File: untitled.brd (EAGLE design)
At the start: 160 x 100 mm, 33 parts, among them J2 1x3 RA Female .1", U1 SI4463-C2A-GM, U2 ATSAMD21G-M

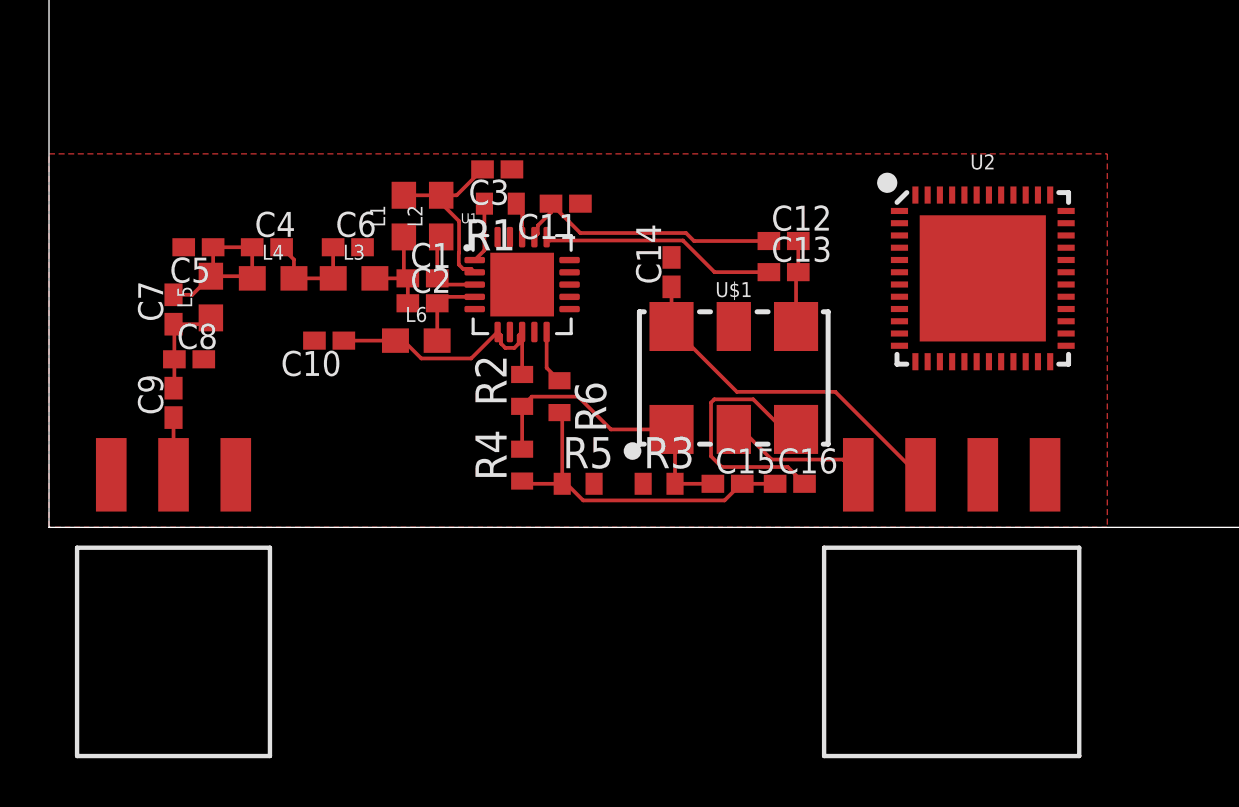
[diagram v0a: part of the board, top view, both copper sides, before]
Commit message: initial atsamd21g schematic capture
added samd21g connections.
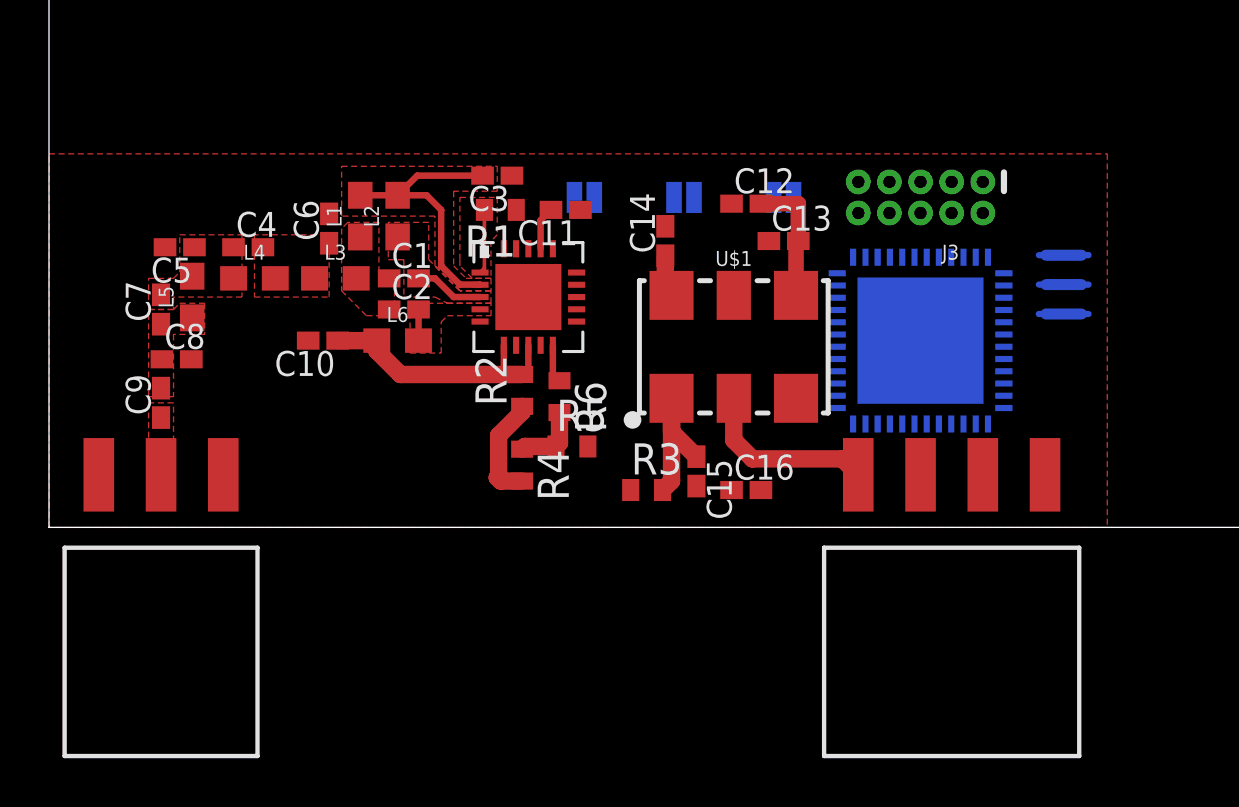
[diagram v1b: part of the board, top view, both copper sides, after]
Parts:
- removed U1: SI4463-C2A-GM, SI4463-C2A-GM:QFN50P400X400X90-20N
- added J3: CORTEX_DEBUG_PTH, SparkFun-Connectors:2X5-PTH-1.27MM
- added REGION1, REGION2, REGION3: JUMPER-SMT_2_NO_SILK, SparkFun-Jumpers:SMT-JUMPER_2_NO_SILK
- added U$2: SI4464, Ava:QFN20+GNDPAD
- added Y1: (no value), SparkFun-Clocks:RESONATOR-SMD-3.2X1.3
- moved U2 3.59 mm to (35.6, 7.62), flipped to the bottom
- moved C12 2.16 mm to (28.4, 13.2)
- moved C16 1.80 mm to (28.4, 1.52)
- moved L1 1.78 mm to (12.7, 12.7)
- moved L2 1.78 mm to (14.2, 12.7)
- moved R5 1.55 mm to (21.3, 3.30)
- moved C15 1.37 mm to (26.4, 2.29), turned to 270 degrees
- moved C14 1.30 mm to (25.1, 11.7)
- moved C13 1.27 mm to (30.0, 11.7)
- moved U$1 1.27 mm to (27.9, 7.37)
- moved C6 1.08 mm to (11.4, 12.2), turned to 90 degrees
- moved C2 0.80 mm to (14.5, 8.89)
- moved C1 0.76 mm to (14.5, 10.2)
- moved C4 0.76 mm to (8.13, 11.4)
- moved C5 0.76 mm to (5.33, 11.4)
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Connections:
- new net !RESET: J3.10, U2.40
- new net A0: U2.3
- new net A1: U2.7
- new net A2: U2.8
- new net A3: U2.9
- new net A4: U2.10
- new net A5: U2.47
- new net AREF: U2.4
- new net D0: U2.16
- new net D1: U2.15
- new net D10: U2.27
- new net D11: U2.25
- new net D12: U2.28
- new net D13: U2.26
- new net D2: U2.23
- new net D3: U2.14
- new net D4: U2.13
- new net D5: U2.24
- new net D6: U2.29
- new net D7: U2.30
- new net D8: U2.11
- new net D9: U2.12
- new net KEY: J3.7
- new net MISO: U2.21
- new net MOSI: U2.19
- new net N$17: J3.6
- new net N$18: J3.8
- new net N$21: U2.48
- new net N$24: U2.5
- new net N$32: U2.22
- new net N$45: U2.39
- new net N$46: U2.41
- new net N$7: U2.2, Y1.3
- new net N$8: U2.1, Y1.1
- new net NC: U$2.5
- new net SCK: U2.20
- new net SCL: U2.32
- new net SDA: U2.31
- new net SRX: U2.38
- new net STX: U2.37
- new net SWCLK: U2.45
- new net SWDCLK: J3.4
- new net SWDIO: J3.2, U2.46
- new net USB+: U2.34
- new net USB-: U2.33
- net GND: now also J3.3, J3.5, J3.9, U$2.18, U$2.21, Y1.2; no longer U1.18, U1.21
- net GPIO0: now also U$2.9; no longer U1.9
- net GPIO2: now also U$2.19; no longer U1.19
- net GPIO3: now also U$2.20; no longer U1.20
- net MODULATION: now also U$2.10; no longer U1.10
- net NIRQ: now also U$2.11; no longer U1.11
- net NSEL: now also U$2.15; no longer U1.15
- net RADIO_SDN: now also U$2.1; no longer U1.1
- net RXN: now also U$2.3; no longer U1.3
- net RXP: now also U$2.2; no longer U1.2
- net SCLK: now also U$2.12; no longer U1.12
- net SDI: now also U$2.14; no longer U1.14
- net SDO: now also U$2.13; no longer U1.13
- net TX: now also U$2.4; no longer U1.4
- net TXRAMP: now also U$2.7; no longer U1.7
- net VCC: now also J3.1, U$2.6, U$2.8, U2.17, U2.36, U2.43, U2.44, U2.6; no longer U1.6, U1.8
- net XIN: now also U$2.17; no longer U1.17
- net XOUT: now also U$2.16; no longer U1.16
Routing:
- net VCC: track 25.0 -> 12.7 mm
- net GND: track 12.0 -> 0.00 mm
- net N$4: track 13.9 -> 2.87 mm
- net XOUT: track 9.66 -> 0.00 mm
- net XIN: track 11.2 -> 1.76 mm
- net N$3: track 7.65 -> 0.00 mm
- net N$1: track 4.35 -> 0.00 mm
- net N$5: track 4.27 -> 0.00 mm
- net N$2: track 4.12 -> 0.00 mm
- net RXP: track 7.56 -> 11.5 mm
- net RADIO_ANT: track 2.34 -> 0.00 mm
- net TX: track 3.16 -> 1.27 mm
- net OUT: track 3.53 -> 5.30 mm
- net ENABLE: track 5.85 -> 7.37 mm
- net N$6: track 12.4 -> 11.1 mm
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- added copper zone on layer 1, net N$1
- added copper zone on layer 1, net N$2
- added copper zone on layer 1, net N$3
- added copper zone on layer 1, net N$5
- added copper zone on layer 1, net RADIO_ANT
- added copper zone on layer 1, net RADIO_SDN
- added copper zone on layer 1, net RXN
- added copper zone on layer 1, net RXP
- added copper zone on layer 1, net TX
